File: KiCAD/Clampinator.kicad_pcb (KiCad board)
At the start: 4 copper layers, 200 x 115 mm, 197 parts, among them J1 Power, J10 Conn_01x04, J11 Conn_01x04, J12 FDCAN_1, J13 FDCAN_2, J14 10k NTC, J15 10k NTC, J16 EN_NTC_B, J17 EN_NTC_A, J18 FAN, J19 FAN, J20 VP0265840000G, J23 VP0265840000G, J24 VP0265840000G, J25 +5V INJ, J26 UART4, J5 Debug Header, J6 Conn_01x04, J7 Conn_01x04, J8 Conn_01x04, J9 Conn_01x04, Q1 TK100E10N1,S1X, Q10 AO3400A, Q2 TK100E10N1,S1X, Q3 TK100E10N1,S1X, Q4 TK100E10N1,S1X, Q5 TK100E10N1,S1X, Q9 MMBT3904-C20526, SW1 PTS810SJM250SMTRLFS, SW2 PTS810SJM250SMTRLFS, SW3 PTS810SJM250SMTRLFS, SW4 PTS810SJM250SMTRLFS, SW5 SMQS-02R-TP, SW6 EG1847-ND, SW7 GPI-154-3013, U1 STM32H573RIT6, U10 LM74810QDRRRQ1, U12 TPS7A2033DQNR, U13 VOS618A-3T, U14 LM5163DDAR, U2 TL432BQDBZR, U3 EG2131, U4 UCC33420RAQR_C46461551, U5 USBLC6-2SC6, U6 LM5012DDAR, U7 MCP2562FD-E/P, U8 MCP2562FD-E/P, U9 EL357N, X1 SC-32S32.768kHz20PPM7pF, Y2 ECS-80-18-23B-JTM-TR

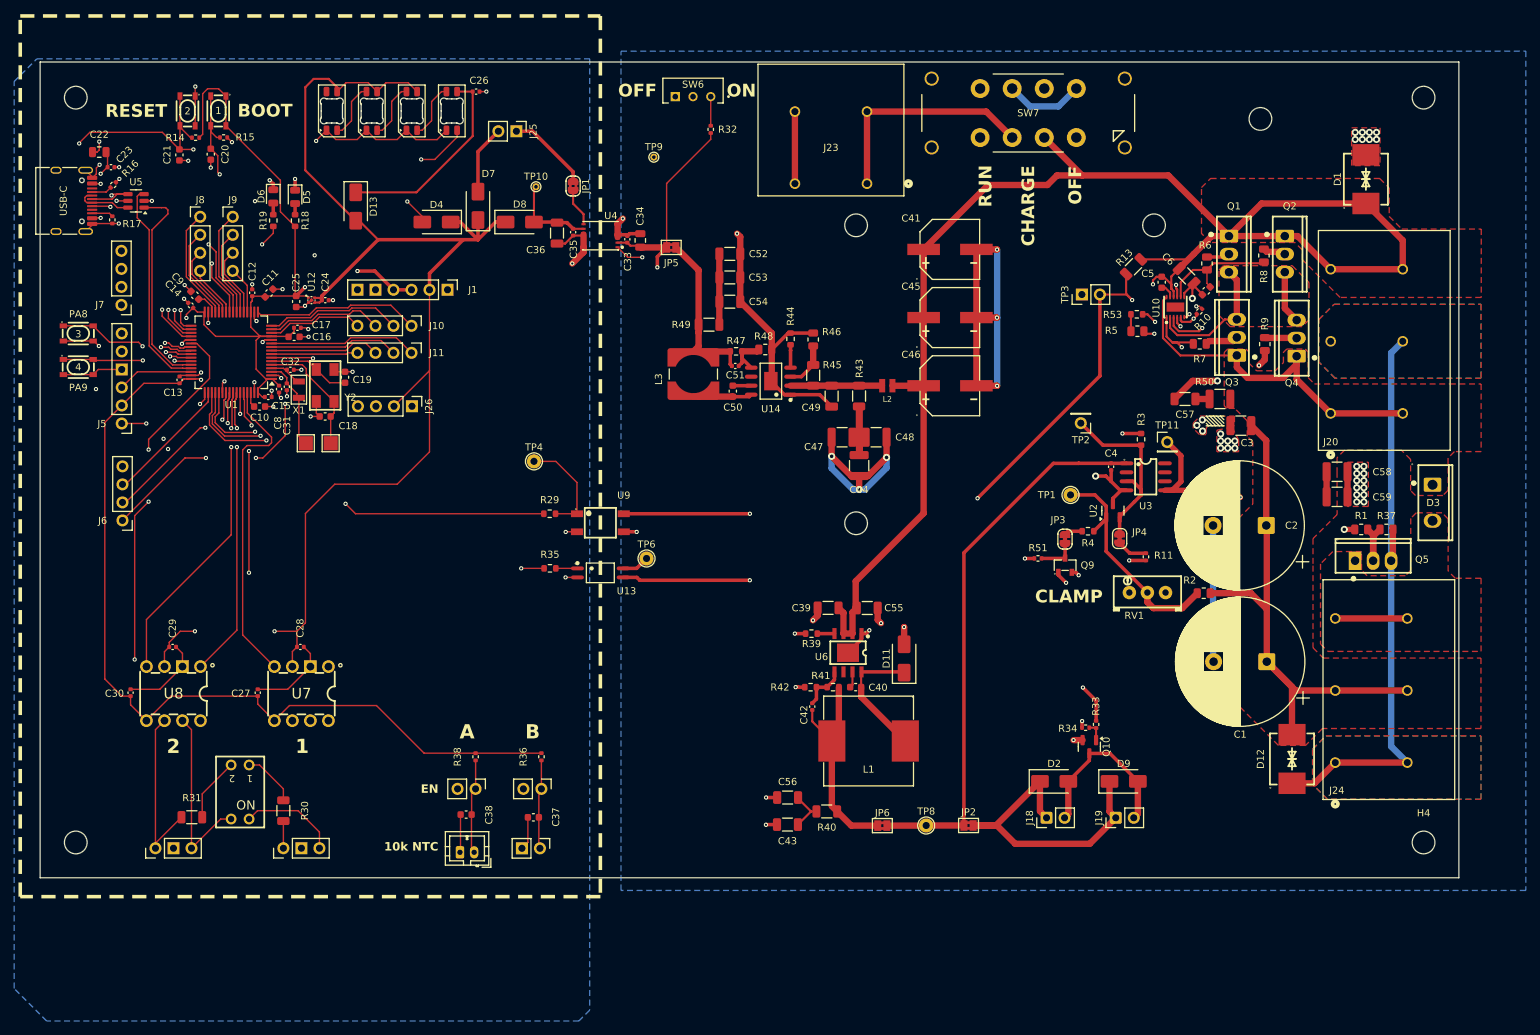
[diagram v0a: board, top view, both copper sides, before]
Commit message: Resolve DRC errors, cleanup traces, nudge footprints for hand soldering
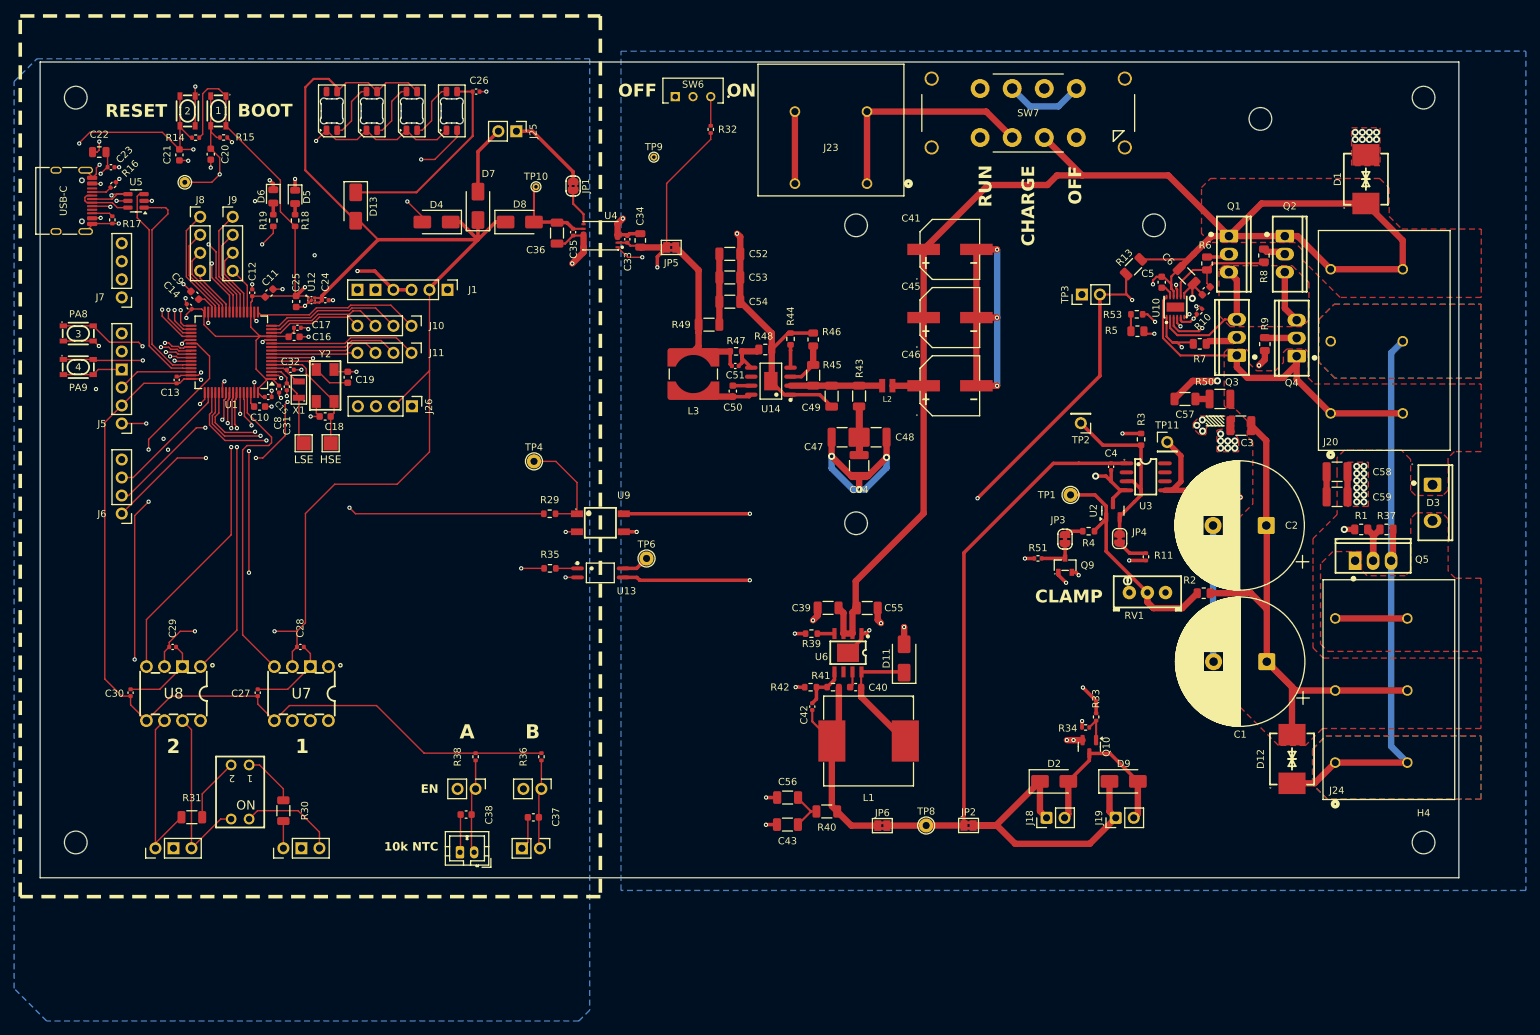
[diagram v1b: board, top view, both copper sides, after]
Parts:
- added TP12: BOOT, TestPoint:TestPoint_THTPad_D1.5mm_Drill0.7mm, F.Cu at (68.2, 41.5)
- moved J7 1.07 mm to (59.3, 57.7)
- moved R33 1.05 mm to (196.7, 116.9)
- moved J6 0.97 mm to (59.3, 88.2)
- moved C13 0.41 mm to (67.0, 69.3)
- moved C19 0.39 mm to (91.2, 69.0)
- moved TP5 0.30 mm to (85.0, 78.3)
- moved C14 0.26 mm to (68.8, 59.0)
- moved R4 0.09 mm to (195.6, 90.7)
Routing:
- net BOOT0: track 57.2 -> 62.5 mm
- net Net-(Q10-G): track 2.70 -> 4.13 mm
- net Net-(R33-Pad2): track 76.7 -> 75.7 mm
- net PB12: track 15.2 -> 16.3 mm
- net GND: track 150.7 -> 151.6 mm
- net PC9: track 41.0 -> 40.0 mm
- net DC_GND: track 298.2 -> 299.1 mm, vias 54 -> 55
- net +5VS: track 191.0 -> 191.9 mm
- net PB13: track 14.2 -> 15.0 mm
- net PB14: track 13.2 -> 13.8 mm
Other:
- board text added: "HSE"
- board text added: "LSE"

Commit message: Added pin silkscreen labels, nudged existing labels for readability
Most of the pin labels say `PWR` for now
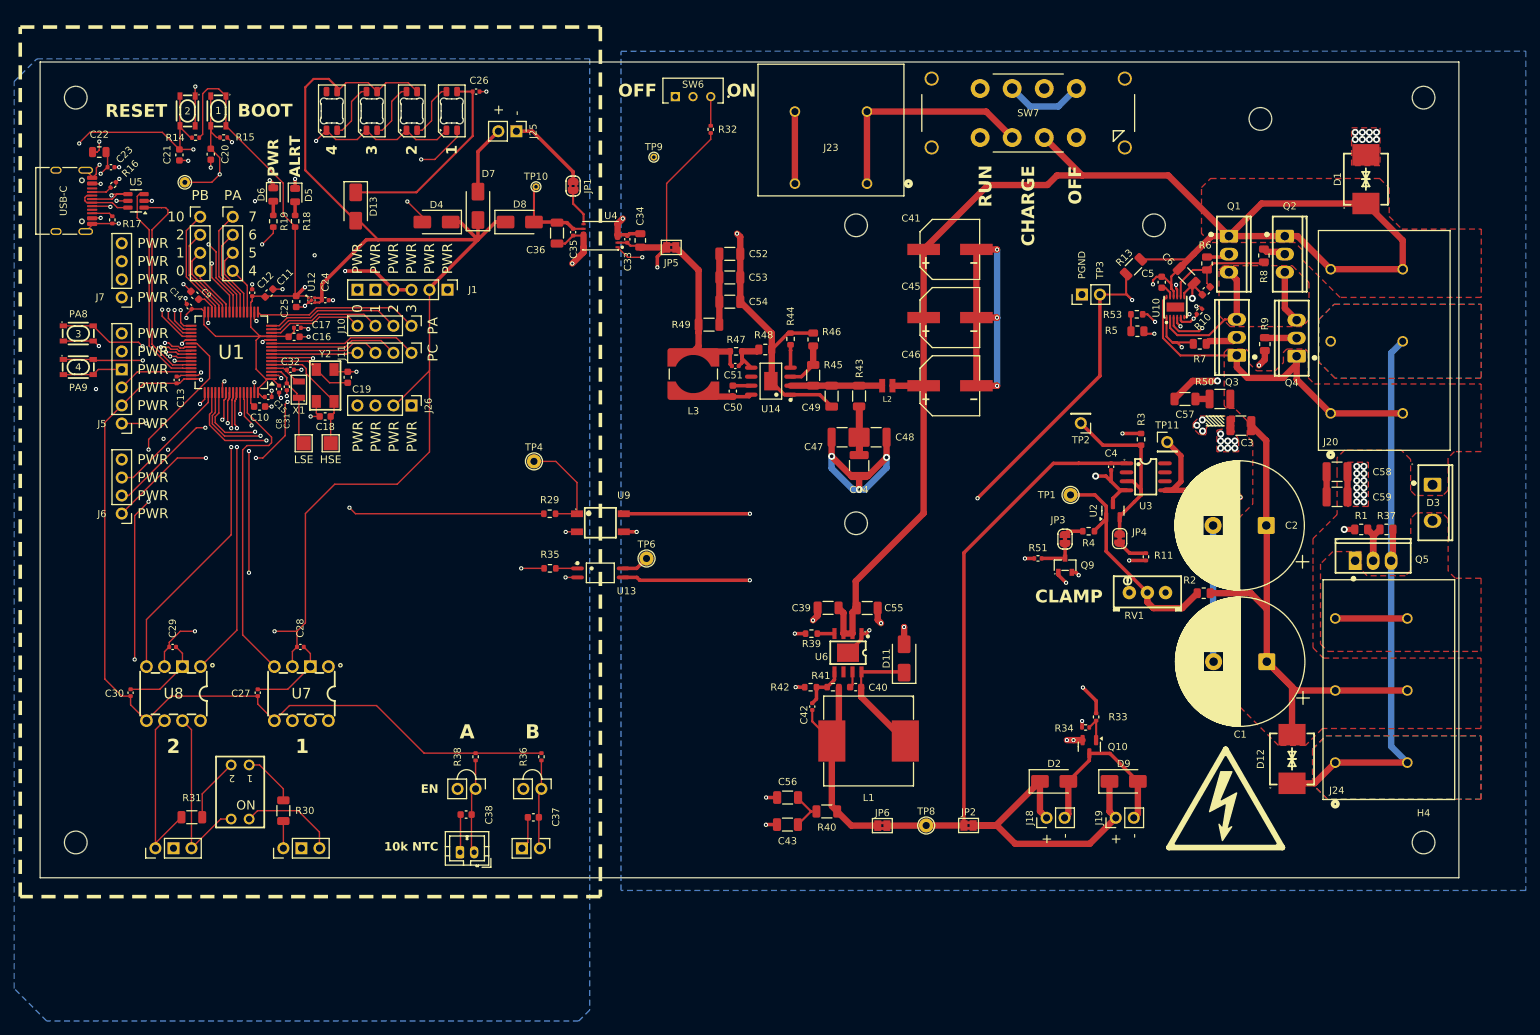
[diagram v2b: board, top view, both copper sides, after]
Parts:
- added REF**: Symbol_HighVoltage_Triangle_17x15mm_Copper, Symbol:Symbol_HighVoltage_Triangle_17x15mm_Copper, F.Cu at (214.9, 128.3)
- added REF**: Symbol_HighVoltage_Triangle_8x7mm_Copper, Symbol:Symbol_HighVoltage_Triangle_8x7mm_Copper, B.Cu at (214.8, 129.5)
- moved D5 0.26 mm to (83.7, 43.3)
- moved D6 0.26 mm to (80.7, 43.2)
- moved J26 0.13 mm to (100.2, 72.9)
- moved R18 0.10 mm to (83.8, 47.0)
- moved R19 0.10 mm to (80.7, 47.0)
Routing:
- net +5VS: track 191.9 -> 192.9 mm
- net GND: track 151.6 -> 151.1 mm
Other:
- board text added: "+"
- board text added: "-"
- board text added: "0"
- board text added: "10"
- board text added: "5"
- board text added: "6"
- board text added: "7"
- board text added: "ALRT"
- board text added: "PA"
- board text added: "PB"
- board text added: "PC"
- board text added: "PGND"
- board text added: "PWR"

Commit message: Fill in labels and align capacitors
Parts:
- moved C1 0.07 mm to (220.7, 109.1)
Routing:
- net BRAKE_A: track 379.9 -> 374.9 mm
- net DC_GND: track 299.1 -> 300.0 mm
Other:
- board text added: "3V3"
- board text added: "5V"
- board text added: "A15"
- board text added: "B12"
- board text added: "B13"
- board text added: "B14"
- board text added: "B15"
- board text added: "B4"
- board text added: "BRAKE +"
- board text added: "BRAKE -"
- board text added: "C13"
- board text added: "C9"
- board text added: "CLK"
- board text added: "DIO"
- board text added: "GND"
- board text added: "NRST"
- board text added: "RX C11"
- board text added: "SWO"
- board text added: "TX C10"
- board text removed: "Brake+"
- board text removed: "Brake-"

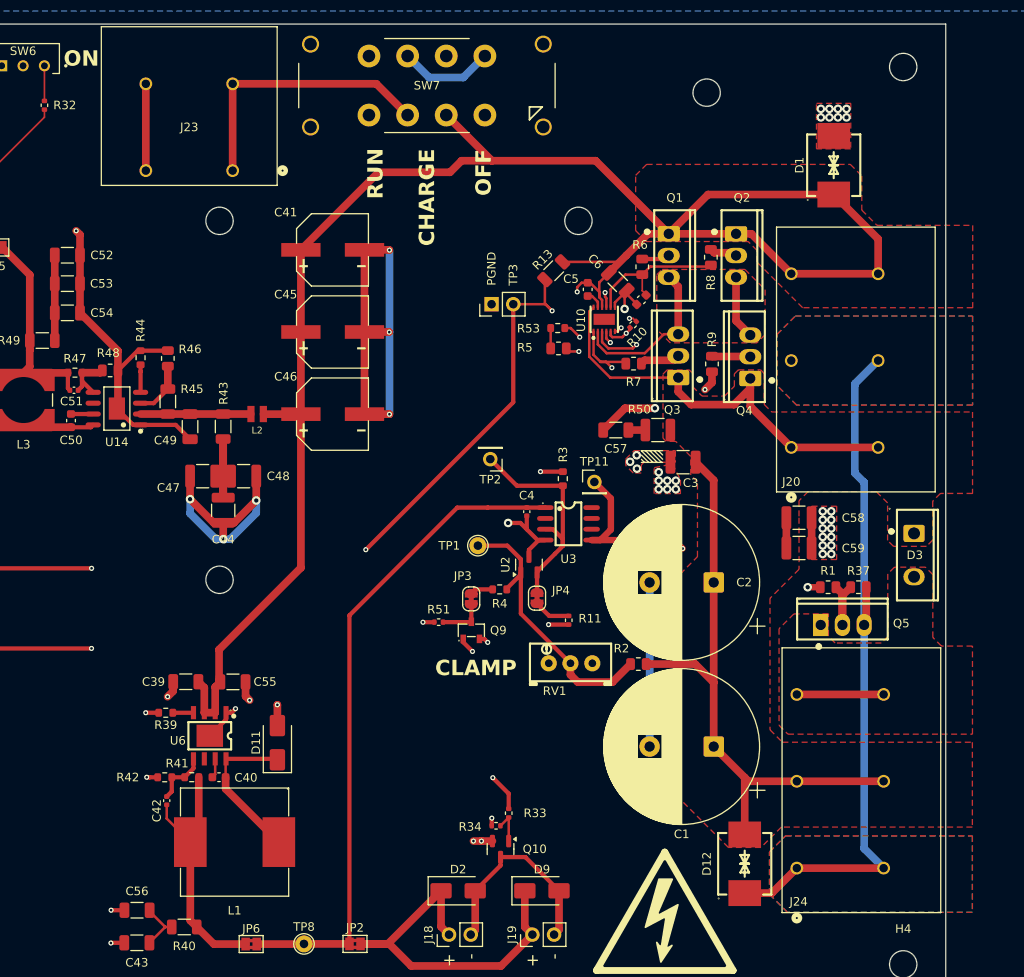
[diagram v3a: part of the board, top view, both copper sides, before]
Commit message: Swap out input TVS for 14S maximum, relinked easyeda2kicad library, added extra shunting NMOS (DNP-ed)
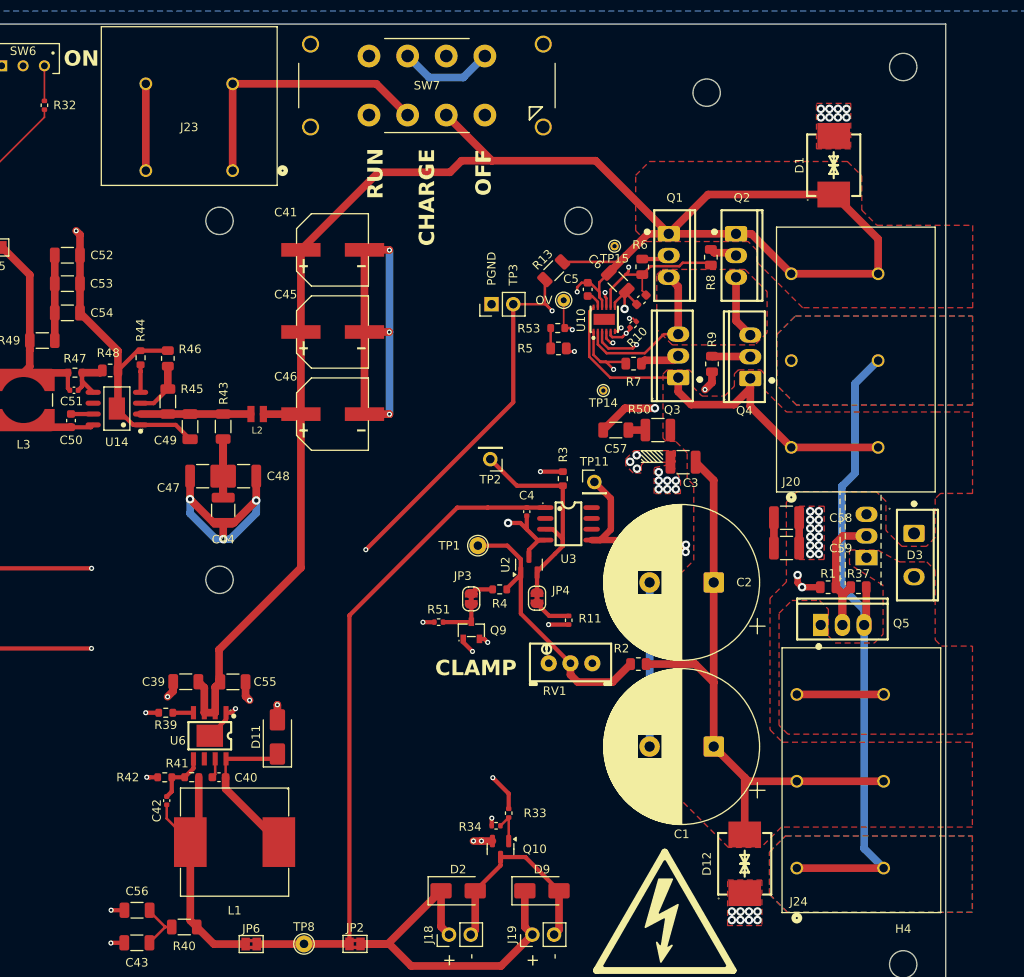
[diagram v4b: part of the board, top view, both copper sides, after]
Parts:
- added Q6: TK100E10N1,S1X, easyeda2kicad:TO-220-3_L10.0-W4.5-P2.54-L, F.Cu at (238.5, 84.4)
- added TP13: TestPoint, TestPoint:TestPoint_THTPad_D1.5mm_Drill0.7mm, F.Cu at (203.1, 56.9)
- added TP14: D, TestPoint:TestPoint_THTPad_D1.0mm_Drill0.5mm, F.Cu at (207.7, 67.4)
- added TP15: H, TestPoint:TestPoint_THTPad_D1.0mm_Drill0.5mm, F.Cu at (209.1, 50.5)
- D1: value SMCJ60CA -> SMCJ54CA
- moved REF** 30.1 mm to (216.9, 99.5)
- moved C58 1.46 mm to (229.2, 82.3)
- moved C59 1.46 mm to (229.2, 85.8)
- moved D11 0.67 mm to (169.6, 107.9)
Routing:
- net Net-(Q5-G): track 9.55 -> 18.6 mm
- net DC_GND: track 300.0 -> 293.3 mm, vias 55 -> 63
- net Net-(U3-LO): track 38.2 -> 44.0 mm, vias 2 -> 4
- net HGATE: track 17.6 -> 22.0 mm, vias 0 -> 1
- net Net-(U10-OV): track 11.2 -> 14.5 mm
- net DGATE: track 23.3 -> 26.3 mm
- net Net-(U10-SW): track 7.24 -> 7.84 mm
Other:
- board text added: "OV"
